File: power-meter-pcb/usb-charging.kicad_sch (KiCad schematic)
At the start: 29 parts, among them J3 USB4120-03-C_REVA, Q1 AS2302, Q2 AS2302, U3 MCP73831-2-OT, U4 TPD3E001DRLR, U5 S-8261AAJMD-G2JT2U, U6 TPS63031DSK

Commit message: Routing and component placement continues
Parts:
- added D4: D, Diode_SMD:D_0603_1608Metric_Pad1.05x0.95mm_HandSolder, symbol Device:D
- J4: renamed from BT1; footprint Connector_JST:JST_EH_B2B-EH-A_1x02_P2.50mm_Vertical -> Connector_JST:JST_PH_B2B-PH-K_1x02_P2.00mm_Vertical
- renumbered C9 to C10, C10 to C11, C6 to C5, C5 to C6, C15 to C9, R8 to R10, R9 to R11, R10 to R12, R12 to R13, R11 to R14, R19 to R15, R5 to R7, R6 to R8, R7 to R9
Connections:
- net at D3.1 (K), U3.1 (STAT): now also D4.1 (K)
- new net Charging: D4.2 (A)
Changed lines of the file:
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@@
 	)
 	(junction
+		(at 82.55 151.13)
+		(diameter 0)
+		(color 0 0 0 0)
+	)
+	(junction
 		(at 267.97 49.53)
 		(diameter 0)
@@
 		)
 	)
+	(bus
+		(pts
+			(xy 93.98 57.15) (xy 93.98 58.42)
+		)
+		(stroke
+			(width 0)
+			(type default)
+		)
+	)
 	(wire
 		(pts
@@
 	(wire
 		(pts
+			(xy 92.71 151.13) (xy 95.25 151.13)
+		)
+		(stroke
+			(width 0)
+			(type default)
+		)
+	)
+	(wire
+		(pts
 			(xy 39.37 71.12) (xy 39.37 76.2)
 		)
@@
 		)
 	)
+	(bus
+		(pts
+			(xy 33.02 57.15) (xy 33.02 58.42)
+		)
+		(stroke
+			(width 0)
+			(type default)
+		)
+	)
 	(wire
 		(pts
@@
 		)
 	)
+	(bus
+		(pts
+			(xy 124.46 41.91) (xy 124.46 43.18)
+		)
+		(stroke
+			(width 0)
+			(type default)
+		)
+	)
 	(wire
 		(pts
@@
 	(wire
 		(pts
+			(xy 82.55 151.13) (xy 85.09 151.13)
+		)
+		(stroke
+			(width 0)
+			(type default)
+		)
+	)
+	(wire
+		(pts
 			(xy 170.18 128.27) (xy 181.61 128.27)
 		)
@@
 		)
 	)
+	(hierarchical_label "Charging"
+		(shape output)
+		(at 95.25 151.13 0)
+		(fields_autoplaced yes)
+		(effects
+			(font
+				(size 1.27 1.27)
+			)
+			(justify left)
+		)
+	)
 	(hierarchical_label "USB{DP DN}"
 		(shape bidirectional)
@@
 		(dnp no)
 		(fields_autoplaced yes)
-		(property "Reference" "R8"
+		(property "Reference" "R10"
 			(at 87.63 66.0399 0)
 			(effects
@@
 			(project "power-meter-pcb"
 				(path "/73d1dc3f-3725-4767-8c11-2d32e15ee0d6/4fb726d4-a68e-4ad8-a718-58b82440e761"
-					(reference "R8")
+					(reference "R10")
 					(unit 1)
 				)
@@
 		(dnp no)
 		(fields_autoplaced yes)
-		(property "Reference" "R19"
+		(property "Reference" "R15"
 			(at 246.38 43.18 90)
 			(effects
@@
 			(project "power-meter-pcb"
 				(path "/73d1dc3f-3725-4767-8c11-2d32e15ee0d6/4fb726d4-a68e-4ad8-a718-58b82440e761"
-					(reference "R19")
+					(reference "R15")
 					(unit 1)
 				)
@@
 		(dnp no)
 		(fields_autoplaced yes)
-		(property "Reference" "R12"
+		(property "Reference" "R13"
 			(at 222.25 116.8399 0)
 			(effects
@@
 			(project "power-meter-pcb"
 				(path "/73d1dc3f-3725-4767-8c11-2d32e15ee0d6/4fb726d4-a68e-4ad8-a718-58b82440e761"
-					(reference "R12")
+					(reference "R13")
 					(unit 1)
 				)
@@
 		(dnp no)
 		(fields_autoplaced yes)
-		(property "Reference" "#PWR030"
+		(property "Reference" "#PWR032"
 			(at 267.97 52.07 0)
 			(effects
@@
 			(project "power-meter-pcb"
 				(path "/73d1dc3f-3725-4767-8c11-2d32e15ee0d6/4fb726d4-a68e-4ad8-a718-58b82440e761"
-					(reference "#PWR030")
+					(reference "#PWR032")
 					(unit 1)
 				)
@@
 		(dnp no)
 		(fields_autoplaced yes)
-		(property "Reference" "R7"
+		(property "Reference" "R9"
 			(at 85.09 128.2699 0)
 			(effects
@@
 			(project "power-meter-pcb"
 				(path "/73d1dc3f-3725-4767-8c11-2d32e15ee0d6/4fb726d4-a68e-4ad8-a718-58b82440e761"
-					(reference "R7")
+					(reference "R9")
 					(unit 1)
 				)
@@
 	)
 	(symbol
+		(lib_id "Device:D")
+		(at 88.9 151.13 0)
+		(unit 1)
+		(exclude_from_sim no)
+		(in_bom yes)
+		(on_board yes)
+		(dnp no)
+		(fields_autoplaced yes)
+		(property "Reference" "D4"
+			(at 88.9 144.78 0)
+			(effects
+				(font
+					(size 1.27 1.27)
+				)
+			)
+		)
+		(property "Value" "D"
+			(at 88.9 147.32 0)
+			(effects
+				(font
+					(size 1.27 1.27)
+				)
+			)
+		)
+		(property "Footprint" "Diode_SMD:D_0603_1608Metric_Pad1.05x0.95mm_HandSolder"
+			(at 88.9 151.13 0)
+			(effects
+				(font
+					(size 1.27 1.27)
+				)
+				(hide yes)
+			)
+		)
+		(property "Datasheet" "~"
+			(at 88.9 151.13 0)
+			(effects
+				(font
+					(size 1.27 1.27)
+				)
+				(hide yes)
+			)
+		)
+		(property "Description" "Diode"
+			(at 88.9 151.13 0)
+			(effects
+				(font
+					(size 1.27 1.27)
+				)
+				(hide yes)
+			)
+		)
+		(property "Sim.Device" "D"
+			(at 88.9 151.13 0)
+			(effects
+				(font
+					(size 1.27 1.27)
+				)
+				(hide yes)
+			)
+		)
+		(property "Sim.Pins" "1=K 2=A"
+			(at 88.9 151.13 0)
+			(effects
+				(font
+					(size 1.27 1.27)
+				)
+				(hide yes)
+			)
+		)
+		(pin "2"
+		)
+		(pin "1"
+		)
+		(instances
+			(project "power-meter-pcb"
+				(path "/73d1dc3f-3725-4767-8c11-2d32e15ee0d6/4fb726d4-a68e-4ad8-a718-58b82440e761"
+					(reference "D4")
+					(unit 1)
+				)
+			)
+		)
+	)
+	(symbol
 		(lib_id "power:GNDD")
 		(at 48.26 137.16 0)
@@
 		(dnp no)
 		(fields_autoplaced yes)
-		(property "Reference" "R9"
+		(property "Reference" "R11"
 			(at 134.62 149.8599 0)
 			(effects
@@
 			(project "power-meter-pcb"
 				(path "/73d1dc3f-3725-4767-8c11-2d32e15ee0d6/4fb726d4-a68e-4ad8-a718-58b82440e761"
-					(reference "R9")
+					(reference "R11")
 					(unit 1)
 				)
@@
 		(dnp no)
 		(fields_autoplaced yes)
-		(property "Reference" "C10"
+		(property "Reference" "C11"
 			(at 271.78 62.2299 0)
 			(effects
@@
 			(project "power-meter-pcb"
 				(path "/73d1dc3f-3725-4767-8c11-2d32e15ee0d6/4fb726d4-a68e-4ad8-a718-58b82440e761"
-					(reference "C10")
+					(reference "C11")
 					(unit 1)
 				)
@@
 		(dnp no)
 		(fields_autoplaced yes)
-		(property "Reference" "#PWR031"
+		(property "Reference" "#PWR033"
 			(at 267.97 86.36 0)
 			(effects
@@
 			(project "power-meter-pcb"
 				(path "/73d1dc3f-3725-4767-8c11-2d32e15ee0d6/4fb726d4-a68e-4ad8-a718-58b82440e761"
-					(reference "#PWR031")
+					(reference "#PWR033")
 					(unit 1)
 				)
@@
 		(dnp no)
 		(fields_autoplaced yes)
-		(property "Reference" "C6"
+		(property "Reference" "C5"
 			(at 160.02 62.2299 0)
 			(effects
@@
 			(project "power-meter-pcb"
 				(path "/73d1dc3f-3725-4767-8c11-2d32e15ee0d6/4fb726d4-a68e-4ad8-a718-58b82440e761"
-					(reference "C6")
+					(reference "C5")
 					(unit 1)
 				)
@@
 		(dnp no)
 		(fields_autoplaced yes)
-		(property "Reference" "#PWR029"
+		(property "Reference" "#PWR031"
 			(at 222.25 50.8 0)
 			(effects
@@
 			(project "power-meter-pcb"
 				(path "/73d1dc3f-3725-4767-8c11-2d32e15ee0d6/4fb726d4-a68e-4ad8-a718-58b82440e761"
-					(reference "#PWR029")
+					(reference "#PWR031")
 					(unit 1)
 				)
@@
 		(dnp no)
 		(fields_autoplaced yes)
-		(property "Reference" "C9"
+		(property "Reference" "C10"
 			(at 243.84 62.2299 0)
 			(effects
@@
 			(project "power-meter-pcb"
 				(path "/73d1dc3f-3725-4767-8c11-2d32e15ee0d6/4fb726d4-a68e-4ad8-a718-58b82440e761"
-					(reference "C9")
+					(reference "C10")
 					(unit 1)
 				)
@@
 		(dnp no)
 		(fields_autoplaced yes)
-		(property "Reference" "R10"
+		(property "Reference" "R12"
 			(at 166.37 121.92 90)
 			(effects
@@
 			(project "power-meter-pcb"
 				(path "/73d1dc3f-3725-4767-8c11-2d32e15ee0d6/4fb726d4-a68e-4ad8-a718-58b82440e761"
-					(reference "R10")
+					(reference "R12")
 					(unit 1)
 				)
@@
 		(dnp no)
 		(fields_autoplaced yes)
-		(property "Reference" "#PWR045"
+		(property "Reference" "#PWR030"
 			(at 219.71 146.05 0)
 			(effects
@@
 			(project "power-meter-pcb"
 				(path "/73d1dc3f-3725-4767-8c11-2d32e15ee0d6/4fb726d4-a68e-4ad8-a718-58b82440e761"
-					(reference "#PWR045")
+					(reference "#PWR030")
 					(unit 1)
 				)
@@
 		(dnp no)
 		(fields_autoplaced yes)
-		(property "Reference" "BT1"
+		(property "Reference" "J4"
 			(at 185.42 131.5084 0)
 			(effects
@@
 			)
 		)
-		(property "Footprint" "Connector_JST:JST_EH_B2B-EH-A_1x02_P2.50mm_Vertical"
+		(property "Footprint" "Connector_JST:JST_PH_B2B-PH-K_1x02_P2.00mm_Vertical"
 			(at 181.61 133.096 90)
 			(effects
@@
 			(project "power-meter-pcb"
 				(path "/73d1dc3f-3725-4767-8c11-2d32e15ee0d6/4fb726d4-a68e-4ad8-a718-58b82440e761"
-					(reference "BT1")
+					(reference "J4")
 					(unit 1)
 				)
@@
 		(dnp no)
 		(fields_autoplaced yes)
-		(property "Reference" "#PWR046"
+		(property "Reference" "#PWR029"
 			(at 219.71 115.57 0)
 			(effects
@@
 			(project "power-meter-pcb"
 				(path "/73d1dc3f-3725-4767-8c11-2d32e15ee0d6/4fb726d4-a68e-4ad8-a718-58b82440e761"
-					(reference "#PWR046")
+					(reference "#PWR029")
 					(unit 1)
 				)
@@
 		(dnp no)
 		(fields_autoplaced yes)
-		(property "Reference" "R11"
+		(property "Reference" "R14"
 			(at 222.25 129.5399 0)
 			(effects
@@
 			(project "power-meter-pcb"
 				(path "/73d1dc3f-3725-4767-8c11-2d32e15ee0d6/4fb726d4-a68e-4ad8-a718-58b82440e761"
-					(reference "R11")
+					(reference "R14")
 					(unit 1)
 				)
@@
 		(dnp no)
 		(fields_autoplaced yes)
-		(property "Reference" "C15"
+		(property "Reference" "C9"
 			(at 236.22 129.5399 0)
 			(effects
@@
 			(project "power-meter-pcb"
 				(path "/73d1dc3f-3725-4767-8c11-2d32e15ee0d6/4fb726d4-a68e-4ad8-a718-58b82440e761"
-					(reference "C15")
+					(reference "C9")
 					(unit 1)
 				)
@@
 		(dnp no)
 		(fields_autoplaced yes)
-		(property "Reference" "C5"
+		(property "Reference" "C6"
 			(at 161.29 132.0799 0)
 			(effects
@@
 			(project "power-meter-pcb"
 				(path "/73d1dc3f-3725-4767-8c11-2d32e15ee0d6/4fb726d4-a68e-4ad8-a718-58b82440e761"
-					(reference "C5")
+					(reference "C6")
 					(unit 1)
 				)
@@
 		(dnp no)
 		(fields_autoplaced yes)
-		(property "Reference" "R5"
+		(property "Reference" "R7"
 			(at 26.67 58.4199 0)
 			(effects
@@
 			(project "power-meter-pcb"
 				(path "/73d1dc3f-3725-4767-8c11-2d32e15ee0d6/4fb726d4-a68e-4ad8-a718-58b82440e761"
-					(reference "R5")
+					(reference "R7")
 					(unit 1)
 				)
@@
 		(dnp no)
 		(fields_autoplaced yes)
-		(property "Reference" "R6"
+		(property "Reference" "R8"
 			(at 50.8 156.2099 0)
 			(effects
@@
 			(project "power-meter-pcb"
 				(path "/73d1dc3f-3725-4767-8c11-2d32e15ee0d6/4fb726d4-a68e-4ad8-a718-58b82440e761"
-					(reference "R6")
+					(reference "R8")
 					(unit 1)
 				)

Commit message: Improved board outline, in the middle of layout changes
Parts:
- renumbered D3 to D4, D4 to D5, R9 to R10, R10 to R11, R11 to R12, R12 to R13, R13 to R14, R14 to R15, R15 to R16, R7 to R8, R8 to R9
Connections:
- net USB.DN: no longer J3.A7 (D1-), J3.B6 (D2+)
- net USB.DP: no longer J3.A6 (D1+), J3.B7 (D2-)
- new net USB.D_N: J3.A7 (D1-), J3.B6 (D2+)
- new net USB.D_P: J3.A6 (D1+), J3.B7 (D2-)
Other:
- moved on the sheet: R8

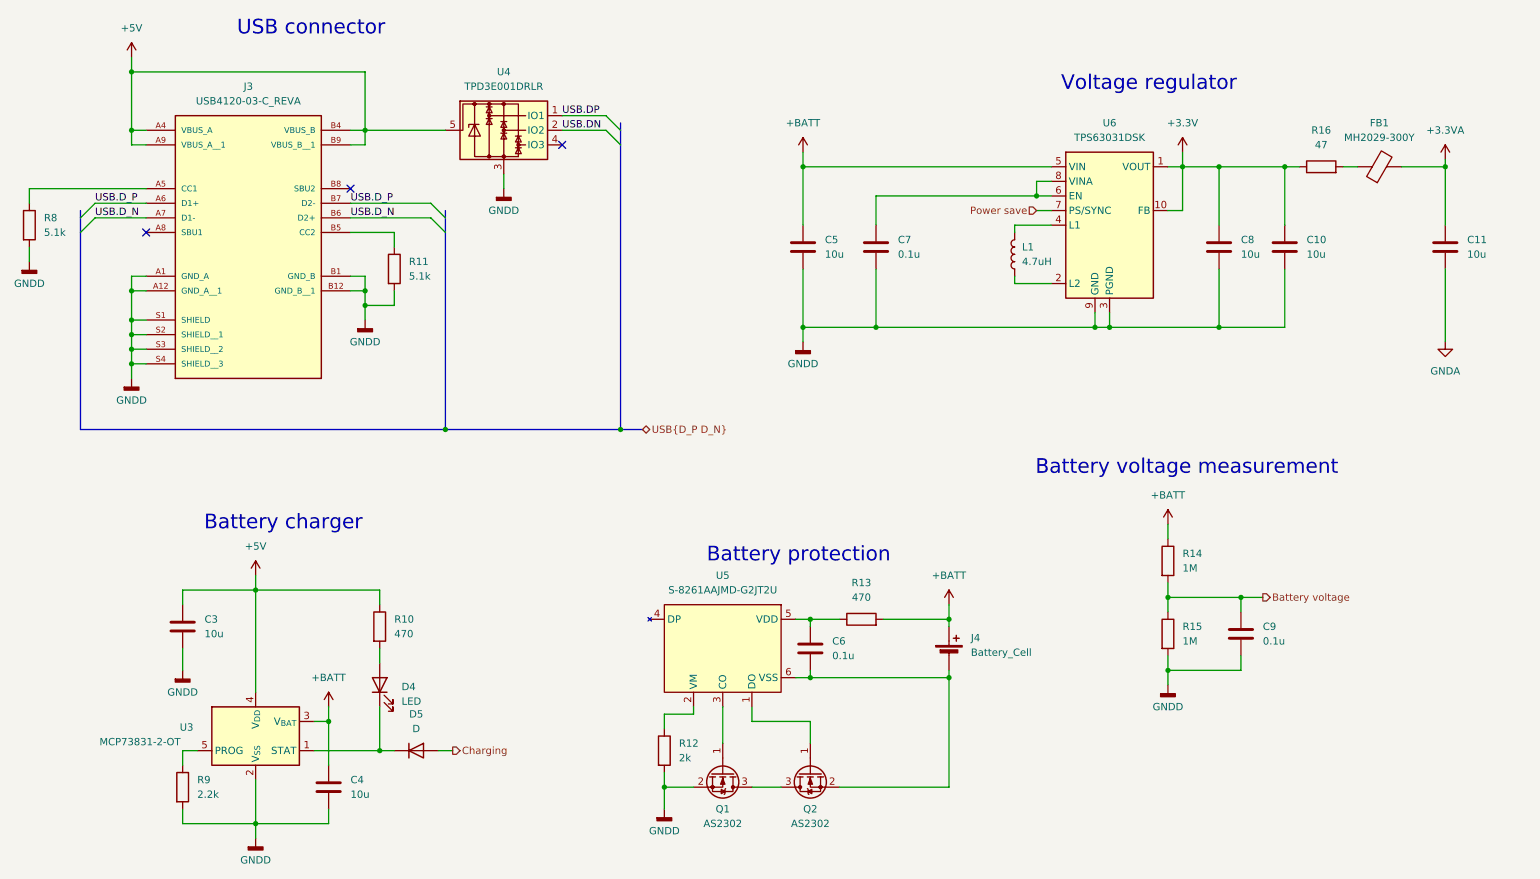
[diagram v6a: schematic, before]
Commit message: Layout almost done, but will likely swap to a 4 layer PCB
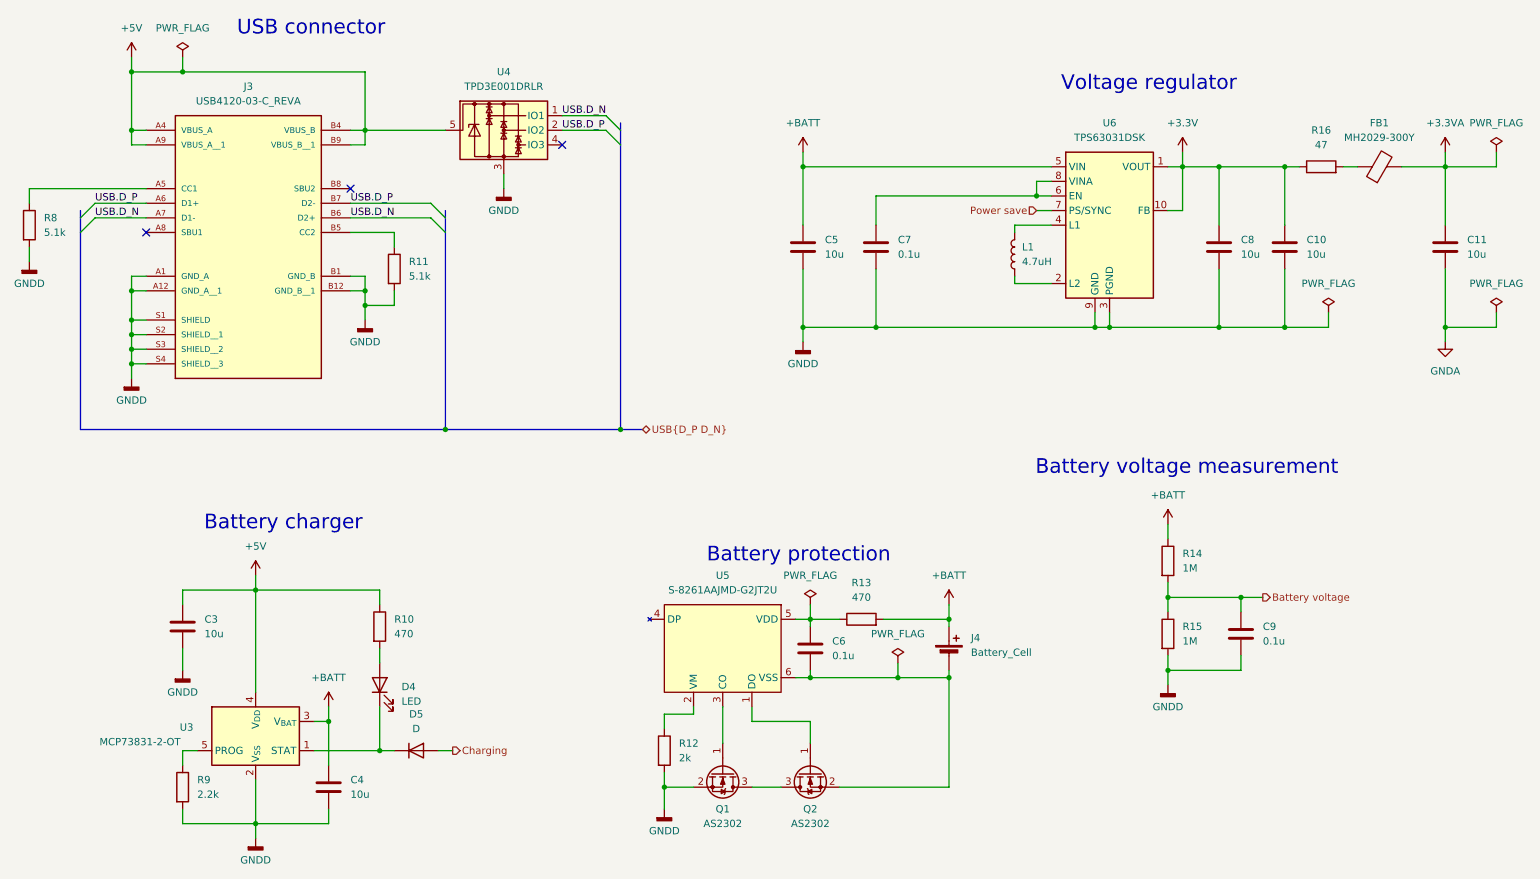
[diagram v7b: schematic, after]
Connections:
- net USB.DN is gone; now on net USB.D_P: U4.2 (IO2)
- net USB.DP is gone; now on net USB.D_N: U4.1 (IO1)

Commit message: Board layout about done, front silkscreen ok
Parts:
- J4: value Battery_Cell -> Battery; footprint Connector_JST:JST_PH_B2B-PH-K_1x02_P2.00mm_Vertical -> Connector_JST:JST_PH_S2B-PH-K_1x02_P2.00mm_Horizontal
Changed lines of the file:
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@@
 			)
 		)
-		(property "Value" "Battery_Cell"
+		(property "Value" "Battery"
 			(at 185.42 134.0484 0)
 			(effects
@@
 			)
 		)
-		(property "Footprint" "Connector_JST:JST_PH_B2B-PH-K_1x02_P2.00mm_Vertical"
+		(property "Footprint" "Connector_JST:JST_PH_S2B-PH-K_1x02_P2.00mm_Horizontal"
 			(at 181.61 133.096 90)
 			(effects
